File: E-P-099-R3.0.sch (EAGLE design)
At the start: 107 parts, among them J1 AVR_ISP, J2 1445055-3, Q1 BSS101, Q2 BSS101, Q3 BSS101, Q4 BSS101, Q5 BSS101, Q6 BSS101

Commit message: added silk screen labels to some parts. moved back to coordinate system origin
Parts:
- removed TE5, TE6, TE7: TE770966, TwoPinWhiteTEConnector:TE770966
- added F1, F2, F3: FUSEMINI-BLADE, Fuse:FUSEMINI-BLADE
- TE1, TE3: value FUSEMINI-BLADE -> TE770966; device Fuse:FUSEMINI-BLADE -> TwoPinWhiteTEConnector:TE770966
- TE2: value TE770966 -> SERVO_PWR
- TE4: value SERVO_PWR -> TE770966
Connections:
- removed net N$65: AT1.D10, JP5.25, JP5.26
- net +12V: now also F1.OUT; no longer TE1.OUT
- net +5V: now also F3.OUT, TE3.V/SIG, TE4.V/SIG; no longer TE5.V/SIG, TE6.V/SIG, TE7.G/LOW
- net BREAK_SWITCH: now also TE3.G/LOW; no longer TE5.G/LOW
- net FREE: now also AT1.D10, JP5.25, JP5.26
- net GND: now also TE1.G/LOW; no longer TE4.G/LOW
- net N$29: now also F2.IN, TE2.V/SIG; no longer TE3.IN, TE4.V/SIG
- net N$47: now also F1.IN, TE1.V/SIG; no longer TE1.IN, TE2.V/SIG
- net N$6: now also F3.IN; no longer TE7.V/SIG
- net SERVO_V: now also F2.OUT; no longer TE3.OUT
- net WIPER_SWITCH: now also TE4.G/LOW; no longer TE6.G/LOW

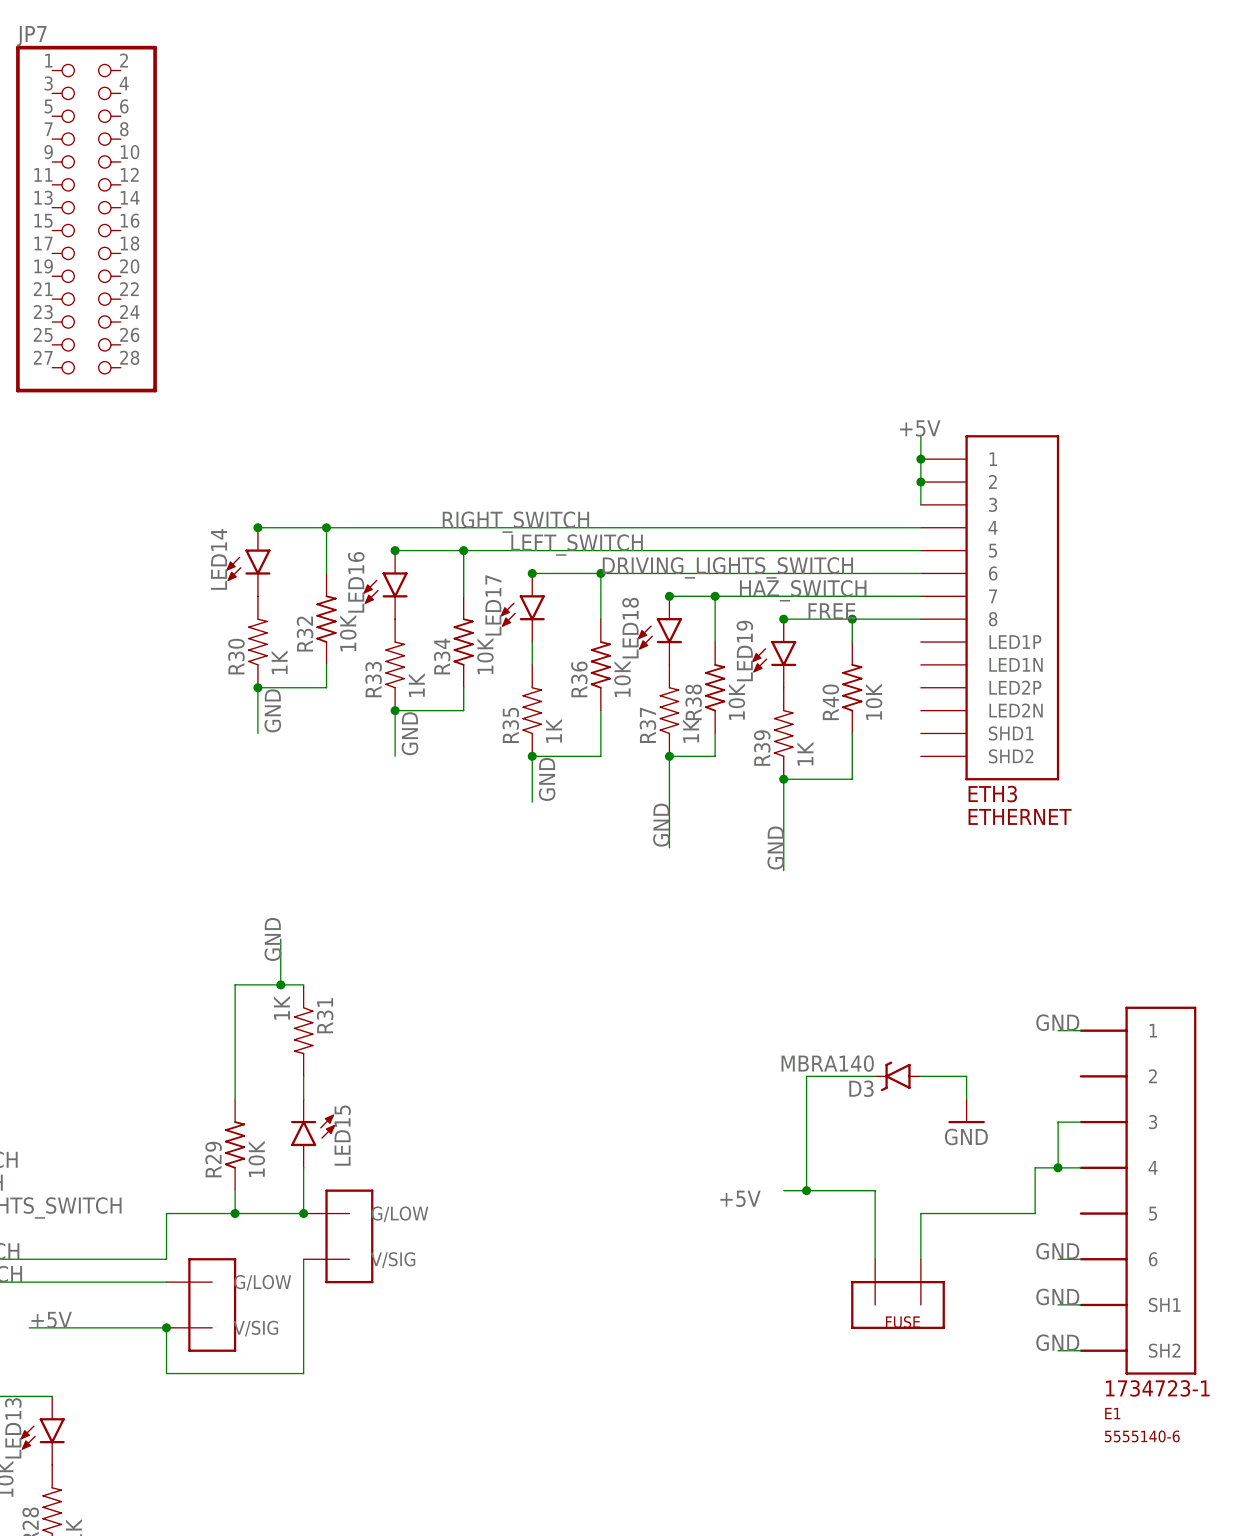
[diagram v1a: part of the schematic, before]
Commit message: took some signals off of steering wheel and put on new ethernet
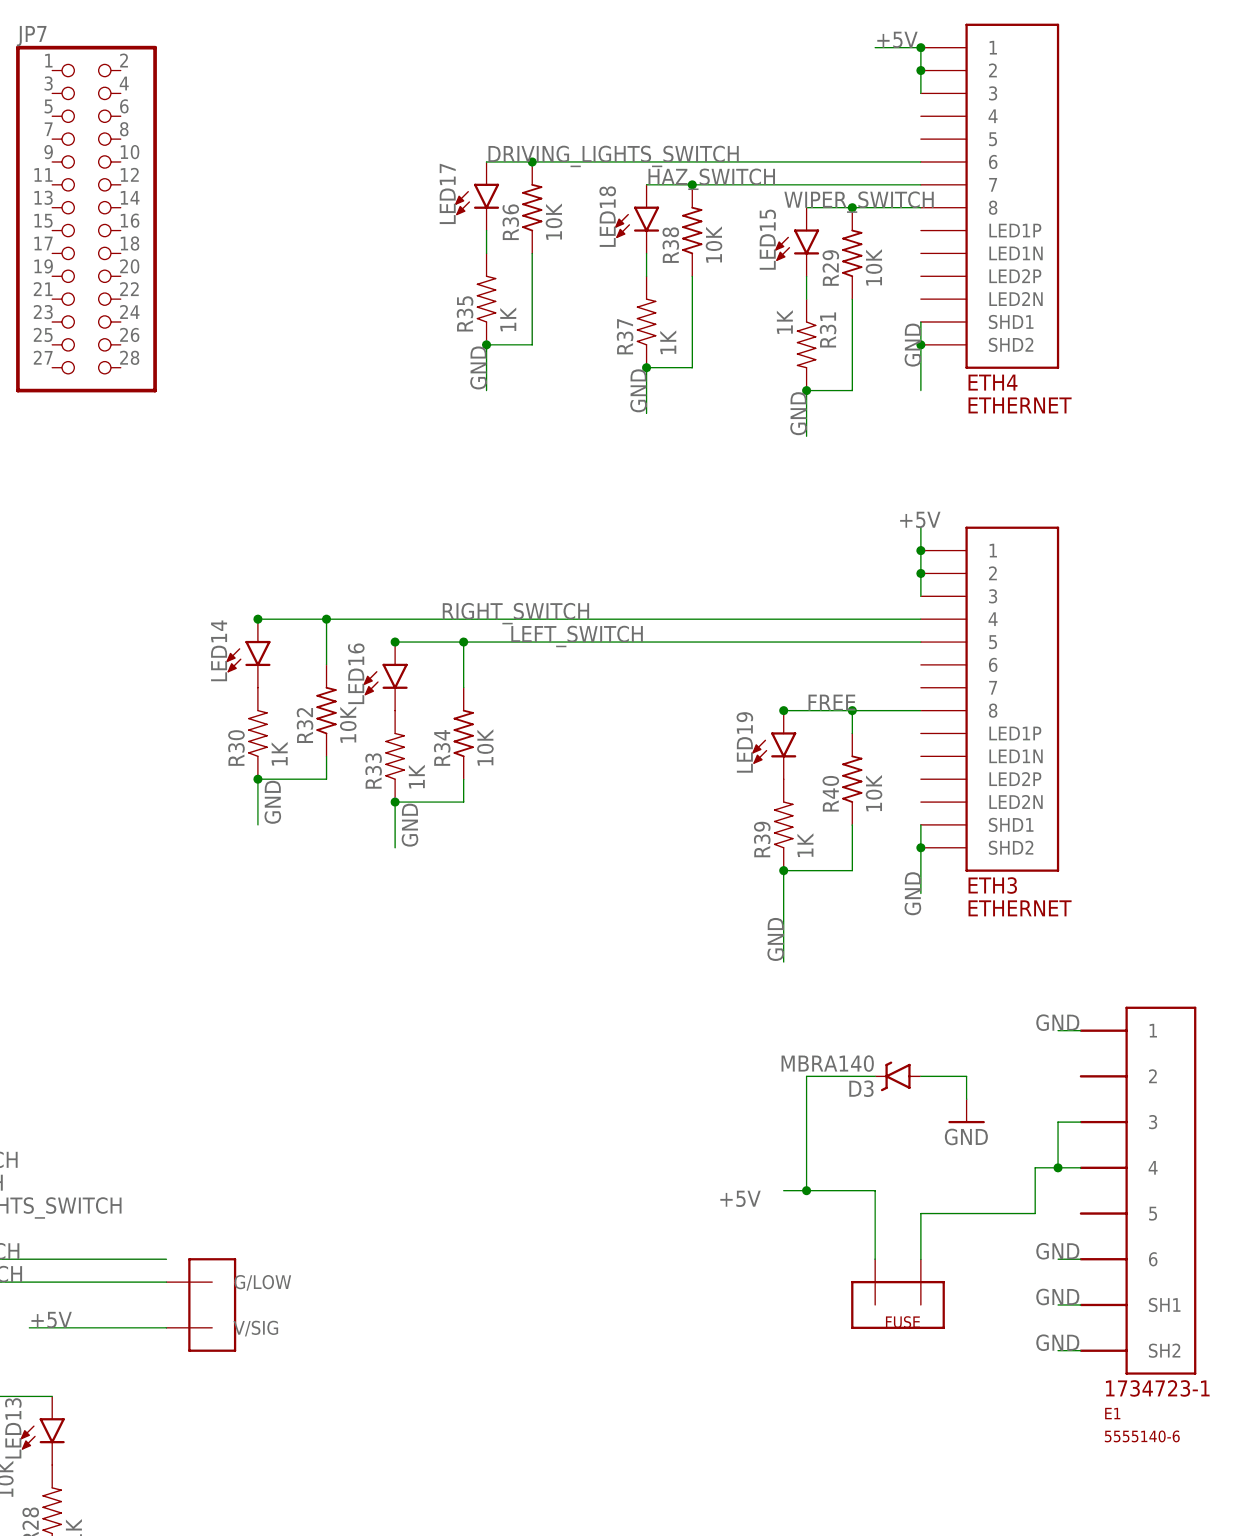
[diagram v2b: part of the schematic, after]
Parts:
- removed TE4: TE770966, TwoPinWhiteTEConnector:TE770966
- added ETH4: ETHERNET, ETHERNET-3:ETHERNET
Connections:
- net +5V: now also ETH4.1, ETH4.2, ETH4.3; no longer TE4.V/SIG
- net DRIVING_LIGHTS_SWITCH: now also ETH4.6; no longer ETH3.6
- net GND: now also ETH3.SHD1, ETH3.SHD2, ETH4.SHD1, ETH4.SHD2, R29.1, R31.2; no longer R29.2, R31.1
- net HAZ_SWITCH: now also ETH4.7; no longer ETH3.7
- net N$28: now also R31.1; no longer R31.2
- net WIPER_SWITCH: now also ETH4.8, R29.2; no longer R29.1, TE4.G/LOW
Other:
- moved on the sheet: ETH3, LED14, LED15, LED16, LED17, LED18, LED19, R29, R30, R31, R32, R33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

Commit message: update
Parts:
- removed LED7, LED8, LED9: (no value), SparkFun-LED:LED0603
- removed R14, R17, R19: 430, SparkFun-Passives:RESISTOR0805-RES
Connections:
- removed net N$41: LED8.C, R17.1
- removed net N$42: LED9.C, R19.1
- removed net N$44: LED7.C, R14.1
- net BRK_L_HIGH: no longer LED9.A
- net BRK_R_HIGH: no longer LED8.A
- net DRIVING_LIGHTS: no longer LED7.A
- net GND: no longer R14.2, R17.2, R19.2
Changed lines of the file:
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@@
 <part name="LED12" library="SparkFun-LED" deviceset="LED" device="0603"/>
 <part name="R26" library="SparkFun-Passives" deviceset="RESISTOR" device="0805-RES" value="430"/>
-<part name="R17" library="SparkFun-Passives" deviceset="RESISTOR" device="0805-RES" value="430"/>
-<part name="LED9" library="SparkFun-LED" deviceset="LED" device="0603"/>
-<part name="R19" library="SparkFun-Passives" deviceset="RESISTOR" device="0805-RES" value="430"/>
-<part name="LED7" library="SparkFun-LED" deviceset="LED" device="0603"/>
-<part name="R14" library="SparkFun-Passives" deviceset="RESISTOR" device="0805-RES" value="430"/>
 <part name="R37" library="SparkFun-Passives" deviceset="RESISTOR" device="0805-RES" value="1K"/>
 <part name="ETH2" library="ETHERNET-3" deviceset="ETHERNET" device=""/>
@@
 <part name="GND3" library="E14-P-099-R21.2(US_drills)" deviceset="GND" device=""/>
 <part name="GND5" library="E14-P-099-R21.2(US_drills)" deviceset="GND" device=""/>
-<part name="LED8" library="SparkFun-LED" deviceset="LED" device="0603"/>
 <part name="LED18" library="SparkFun-LED" deviceset="LED" device="0603"/>
 <part name="JP7" library="E-P-099-R2.2" deviceset="PINHD-2X14" device=""/>
@@
 <instance part="LED12" gate="G$1" x="292.1" y="35.56"/>
 <instance part="R26" gate="G$1" x="281.94" y="40.64" rot="R180"/>
-<instance part="R17" gate="G$1" x="127" y="12.7"/>
-<instance part="LED9" gate="G$1" x="137.16" y="53.34" rot="R180"/>
-<instance part="R19" gate="G$1" x="137.16" y="63.5" rot="R90"/>
-<instance part="LED7" gate="G$1" x="119.38" y="86.36" rot="R180"/>
-<instance part="R14" gate="G$1" x="119.38" y="99.06" rot="R90"/>
 <instance part="R37" gate="G$1" x="363.22" y="241.3" rot="R90"/>
 <instance part="ETH2" gate="G$1" x="129.54" y="246.38"/>
@@
 <instance part="GND3" gate="1" x="27.94" y="83.82"/>
 <instance part="GND5" gate="1" x="35.56" y="83.82"/>
-<instance part="LED8" gate="G$1" x="127" y="22.86"/>
 <instance part="LED18" gate="G$1" x="363.22" y="254"/>
 <instance part="JP7" gate="A" x="299.72" y="254"/>
@@
 <pinref part="GND15" gate="1" pin="GND"/>
 <wire x1="142.24" y1="68.58" x2="137.16" y2="68.58" width="0.1524" layer="91"/>
-<pinref part="R19" gate="G$1" pin="2"/>
-<junction x="137.16" y="68.58"/>
 </segment>
 <segment>
 <pinref part="R20" gate="G$1" pin="2"/>
 <pinref part="GND14" gate="1" pin="GND"/>
-<pinref part="R17" gate="G$1" pin="2"/>
 <wire x1="137.16" y1="12.7" x2="132.08" y2="12.7" width="0.1524" layer="91"/>
-<junction x="132.08" y="12.7"/>
 </segment>
 <segment>
@@
 <pinref part="GND12" gate="1" pin="GND"/>
 <wire x1="124.46" y1="104.14" x2="124.46" y2="96.52" width="0.1524" layer="91"/>
-<pinref part="R14" gate="G$1" pin="2"/>
-<wire x1="119.38" y1="104.14" x2="124.46" y2="104.14" width="0.1524" layer="91"/>
-<junction x="124.46" y="104.14"/>
 </segment>
 <segment>
@@
 <pinref part="R20" gate="G$1" pin="1"/>
 <wire x1="132.08" y1="25.4" x2="137.16" y2="22.86" width="0.1524" layer="91"/>
-<pinref part="LED8" gate="G$1" pin="A"/>
-<junction x="127" y="25.4"/>
 </segment>
 <segment>
@@
 <label x="142.24" y="50.8" size="1.778" layer="95"/>
 <wire x1="137.16" y1="50.8" x2="142.24" y2="50.8" width="0.1524" layer="91"/>
-<pinref part="LED9" gate="G$1" pin="A"/>
-<junction x="137.16" y="50.8"/>
 <pinref part="R21" gate="G$1" pin="2"/>
 <wire x1="142.24" y1="50.8" x2="152.4" y2="50.8" width="0.1524" layer="91"/>
@@
 </segment>
 </net>
-<net name="N$41" class="0">
-<segment>
-<pinref part="R17" gate="G$1" pin="1"/>
-<wire x1="127" y1="17.78" x2="121.92" y2="17.78" width="0.1524" layer="91"/>
-<wire x1="121.92" y1="17.78" x2="121.92" y2="12.7" width="0.1524" layer="91"/>
-<pinref part="LED8" gate="G$1" pin="C"/>
-</segment>
-</net>
-<net name="N$42" class="0">
-<segment>
-<pinref part="LED9" gate="G$1" pin="C"/>
-<pinref part="R19" gate="G$1" pin="1"/>
-</segment>
-</net>
-<net name="N$44" class="0">
-<segment>
-<pinref part="LED7" gate="G$1" pin="C"/>
-<pinref part="R14" gate="G$1" pin="1"/>
-<wire x1="119.38" y1="93.98" x2="119.38" y2="91.44" width="0.1524" layer="91"/>
-</segment>
-</net>
 <net name="RIGHT_SWITCH" class="0">
 <segment>
@@
 <label x="127" y="83.82" size="1.778" layer="95"/>
 <pinref part="R16" gate="G$1" pin="2"/>
-<wire x1="124.46" y1="83.82" x2="119.38" y2="83.82" width="0.1524" layer="91"/>
-<wire x1="119.38" y1="83.82" x2="116.84" y2="83.82" width="0.1524" layer="91"/>
+<wire x1="124.46" y1="83.82" x2="116.84" y2="83.82" width="0.1524" layer="91"/>
 <wire x1="124.46" y1="86.36" x2="124.46" y2="83.82" width="0.1524" layer="91"/>
 <junction x="124.46" y="83.82"/>
-<pinref part="LED7" gate="G$1" pin="A"/>
-<junction x="119.38" y="83.82"/>
-</segment>
-<segment>
+</segment>
+<segment>
